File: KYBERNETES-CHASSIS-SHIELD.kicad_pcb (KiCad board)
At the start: 2 copper layers, 53.3 x 57.1 mm, 29 parts, among them J1 ESC, J2 Radio, J3 Encoder, J4 I2C, J5 Servo 1, J6 Servo 2, J7 Servo Regulator 1, J8 Servo Regulator 2, U1 LM4040CEM3-3.0T, U2 LM2903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

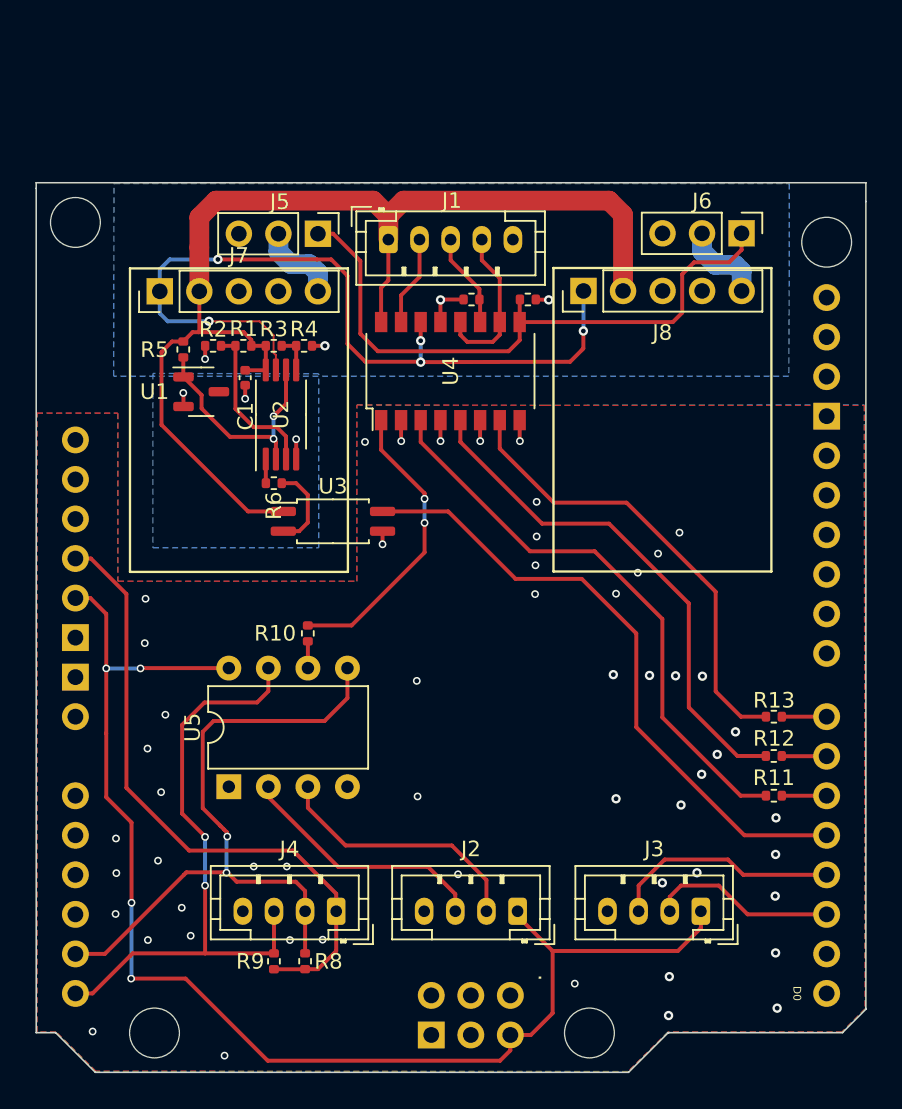
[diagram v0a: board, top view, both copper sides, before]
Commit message: rework into 4 layer board
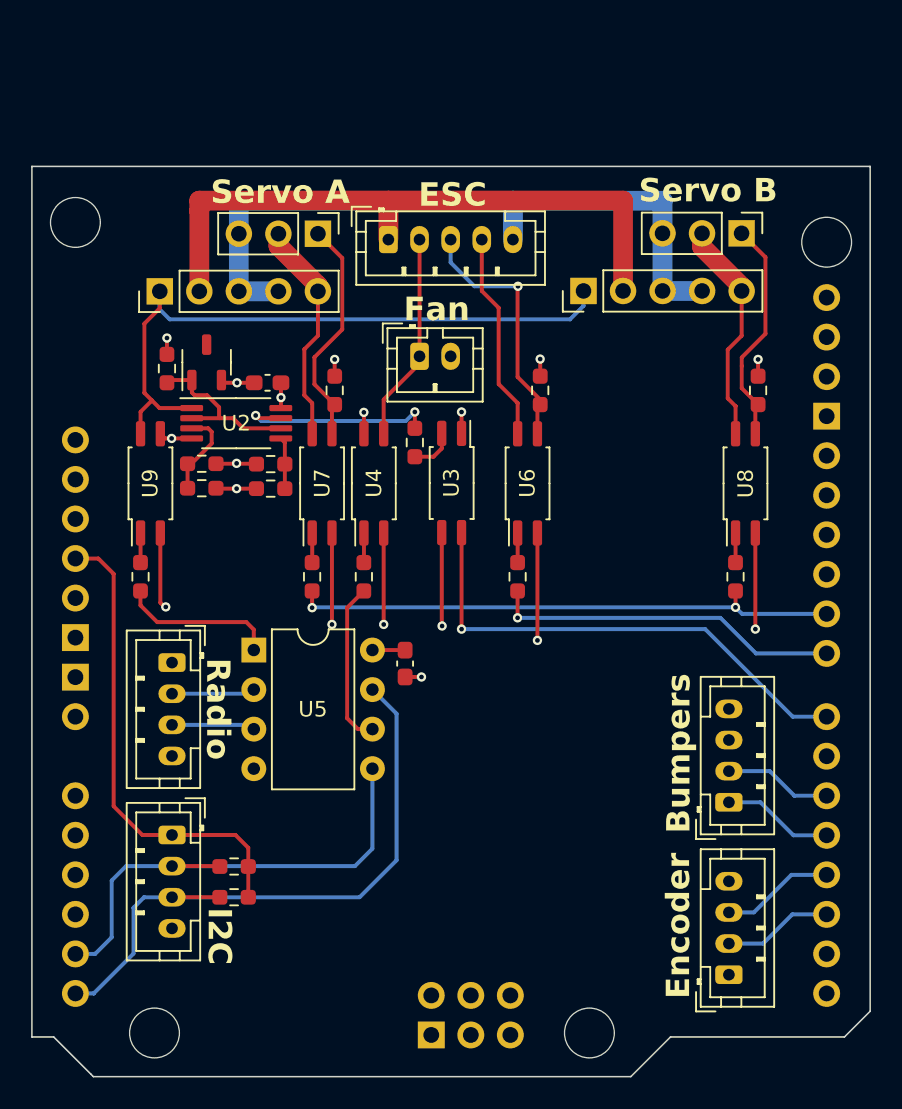
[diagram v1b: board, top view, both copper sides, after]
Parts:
- removed R15: 2k2, Resistor_SMD:R_0402_1005Metric
- added C2: 100n, Capacitor_SMD:C_0603_1608Metric_Pad1.08x0.95mm_HandSolder, F.Cu at (148.8, 105.2)
- added J10: Fan, Connector_JST:JST_PH_B2B-PH-K_1x02_P2.00mm_Vertical, F.Cu at (149.8, 85.5)
- added J5: Bumper, Connector_JST:JST_PH_B4B-PH-K_1x04_P2.00mm_Vertical, F.Cu at (169.7, 114.1)
- added R18: 680, Resistor_SMD:R_0603_1608Metric_Pad0.98x0.95mm_HandSolder, F.Cu at (142.9, 99.6)
- added R19: 680, Resistor_SMD:R_0603_1608Metric_Pad0.98x0.95mm_HandSolder, F.Cu at (131.8, 99.6)
- added R7: 680, Resistor_SMD:R_0603_1608Metric_Pad0.98x0.95mm_HandSolder, F.Cu at (146.2, 99.6)
- added U6: TCMT1104, Package_SO:SOP-4_4.4x2.6mm_P1.27mm, F.Cu at (156.7, 93.6)
- added U7: TCMT1104, Package_SO:SOP-4_4.4x2.6mm_P1.27mm, F.Cu at (143.5, 93.6)
- added U8: TCMT1104, Package_SO:SOP-4_4.4x2.6mm_P1.27mm, F.Cu at (170.7, 93.6)
- added U9: TCMT1104, Package_SO:SOP-4_4.4x2.6mm_P1.27mm, F.Cu at (132.5, 93.6)
- C1: footprint Capacitor_SMD:C_0402_1005Metric -> Capacitor_SMD:C_0603_1608Metric_Pad1.08x0.95mm_HandSolder
- R1, R10, R11, R12, R13, R14, R2, R3, R4, R5, R6, R8, R9: footprint Resistor_SMD:R_0402_1005Metric -> Resistor_SMD:R_0603_1608Metric_Pad0.98x0.95mm_HandSolder
- U4: value TCMT4100 -> TCMT1104; footprint Package_SO:SOP-16_4.4x10.4mm_P1.27mm -> Package_SO:SOP-4_4.4x2.6mm_P1.27mm
- moved R11 30.1 mm to (157.5, 87.6), turned to 90 degrees
- moved J2 27.4 mm to (133.9, 105.1), turned to -90 degrees
- moved R12 20.1 mm to (156.1, 99.6), turned to 90 degrees
- moved R14 15.9 mm to (171.5, 87.6), turned to 90 degrees
- moved R10 15.7 mm to (144.3, 87.6)
- moved J4 11.6 mm to (133.9, 116.2), turned to -90 degrees
- moved R3 10.3 mm to (135.8, 93.9), turned to 180 degrees
- moved R4 10.0 mm to (135.8, 92.3)
- moved R6 9.43 mm to (149.5, 91.0), turned to -90 degrees
- moved R1 9.34 mm to (140.2, 94.0), turned to 0 degrees
- moved R13 9.32 mm to (170.1, 99.6), turned to 90 degrees
- moved U5 8.93 mm to (139.1, 104.3), turned to 0 degrees
- moved U4 8.73 mm to (146.8, 93.6)
- moved R2 8.45 mm to (140.2, 92.4)
- moved U3 8.02 mm to (151.8, 93.6), turned to -90 degrees
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- renumbered J5 to J6, J6 to J7, J7 to J8, J8 to J9
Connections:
- net SERVO_POWER_1 renamed SERVO_1_POWER
- net SERVO_POWER_2 renamed SERVO_2_POWER
- J1 pad 4: +5VP -> ESC_POWER
- J6 pad 1: SERVO_IN -> SERVO_1_IN
- J7 pad 1: SERVO_IN -> SERVO_2_IN
- R10 pad 1: ESC_ENABLE_LOGIC -> SERVO_1_IN
- R10 pad 2: Net-(R10-Pad2) -> GND2
- R11 pad 1: SERVO_DISABLE_LOGIC -> ESC_IN
- R11 pad 2: Net-(R11-Pad2) -> GND2
- R14 pad 1: SERVO_IN -> SERVO_2_IN
- U2 pad 1: Net-(R6-Pad1) -> SERVO_DISABLE
- U2 pad 3: MotorBattLowSense -> MotorBattCritSense
- U2 pad 5: MotorBattCritSense -> MotorBattLowSense
- U2 pad 7: SERVO_DISABLE -> Net-(R6-Pad1)
- U4 pad 1: Net-(R10-Pad2) -> Net-(R7-Pad2)
- U4 pad 3: Net-(R11-Pad2) -> ESC_ENABLE
- U4 pad 4: GND -> +12V
- U5 pad 1: unconnected-(U5-~{RESET}/PB5-Pad1) -> SERVO_DISABLE_LOGIC
- U5 pad 2: RADIO_CH2 -> RADIO_CH1
- U5 pad 3: RADIO_CH1 -> RADIO_CH2
- XA1 pad D4: ~{MotorBattLow} -> BUMPER_A
- XA1 pad D5: SERVO_DISABLE_LOGIC -> BUMPER_B
- XA1 pad D6: ESC_IN_LOGIC -> unconnected-(XA1-PadD6)
- XA1 pad D7: SERVO_IN_LOGIC -> ~{MotorBattLow}
- XA1 pad D8: unconnected-(XA1-PadD8) -> ESC_IN_LOGIC
- XA1 pad D9: unconnected-(XA1-PadD9) -> SERVO_IN_LOGIC
- XA1 pad GND1: GND -> unconnected-(XA1-GND-PadGND1)
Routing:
- net +5V: track 84.2 -> 2.10 mm, vias 4 -> 0
- net GND2: track 8.51 -> 56.6 mm, vias 7 -> 6
- net SERVO_IN: track 40.4 -> 0.00 mm
- net Net-(R11-Pad2): track 36.7 -> 0.00 mm
- net SERVO_IN_LOGIC: track 2.88 -> 35.4 mm, vias 0 -> 2
- net Net-(R12-Pad2): track 33.3 -> 1.90 mm
- net GND: track 6.25 -> 36.8 mm, vias 54 -> 7
- net Net-(R13-Pad2): track 29.8 -> 1.90 mm
- net +12V: track 73.7 -> 49.4 mm, vias 0 -> 5
- net ESC_IN_LOGIC: track 2.89 -> 22.5 mm, vias 0 -> 1
- net Net-(R10-Pad2): track 19.1 -> 0.00 mm, vias 2 -> 0
- net SERVO_1_IN: track 0.00 -> 14.8 mm
- net SERVO_2_IN: track 0.00 -> 14.6 mm
- net ESC_POWER: track 0.00 -> 13.4 mm
- net Net-(R6-Pad1): track 1.55 -> 13.3 mm, vias 0 -> 2
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- added copper zone on In2.Cu, net +12V
- added copper zone on In2.Cu, net +5V
- added copper zone on In1.Cu, net GND
- added copper zone on In1.Cu, net GND2
- removed copper zone on B.Cu, net GND
- removed copper zone on F.Cu, net GND
- removed copper zone on B.Cu, net GND2
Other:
- board size 53.3 x 57.1 mm -> 53.8 x 58.5 mm
- copper layers 2 -> 4
- board text added: "Bumpers"
- board text added: "ESC"
- board text added: "Encoder"
- board text added: "Fan"
- board text added: "I2C"
- board text added: "Radio"
- board text added: "Servo A"
- board text added: "Servo B"

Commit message: version 1.0
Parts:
- moved R10 4.01 mm to (144.3, 91.7)
- moved R11 4.01 mm to (157.5, 91.7)
- moved R14 4.01 mm to (171.5, 91.7)
- moved U4 4.01 mm to (146.8, 97.6)
- moved U6 4.01 mm to (156.7, 97.6)
- moved U7 4.01 mm to (143.5, 97.6)
- moved U8 4.01 mm to (170.7, 97.6)
- moved U9 4.01 mm to (132.5, 97.6)
- moved U3 4.01 mm to (151.8, 97.6)
- moved R18 3.20 mm to (141.9, 102.7), turned to 0 degrees
- moved R12 3.20 mm to (157.0, 102.7), turned to 180 degrees
- moved R13 3.20 mm to (169.2, 102.7), turned to 0 degrees
- moved R7 3.19 mm to (145.3, 102.7), turned to 0 degrees
- moved R19 3.17 mm to (132.8, 102.7), turned to 180 degrees
- moved R6 1.68 mm to (151.0, 91.6)
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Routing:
- net GND: track 36.8 -> 6.29 mm
- net ~{MotorBattLow}: track 32.0 -> 27.6 mm
- net ESC_ENABLE: track 13.4 -> 17.4 mm
- net SERVO_DISABLE: track 42.8 -> 46.8 mm
- net ESC_POWER: track 13.4 -> 17.4 mm
- net SERVO_1_POWER: track 14.5 -> 18.5 mm
- net SERVO_2_POWER: track 14.5 -> 18.5 mm
- net ESC_IN: track 16.6 -> 20.6 mm
- net SERVO_1_IN: track 14.8 -> 18.6 mm
- net ESC_IN_LOGIC: track 22.5 -> 18.8 mm
- net SERVO_2_IN: track 14.6 -> 18.3 mm
- net SERVO_DISABLE_LOGIC: track 10.2 -> 7.27 mm
- net SERVO_IN_LOGIC: track 35.4 -> 37.2 mm
- net ESC_ENABLE_LOGIC: track 10.5 -> 9.10 mm
- net Net-(R6-Pad2): track 2.92 -> 1.94 mm
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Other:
- board text added: "Battery Critical Reference"
- board text added: "Battery Low Reference"
- board text added: "Kybernetes 2 Shield"

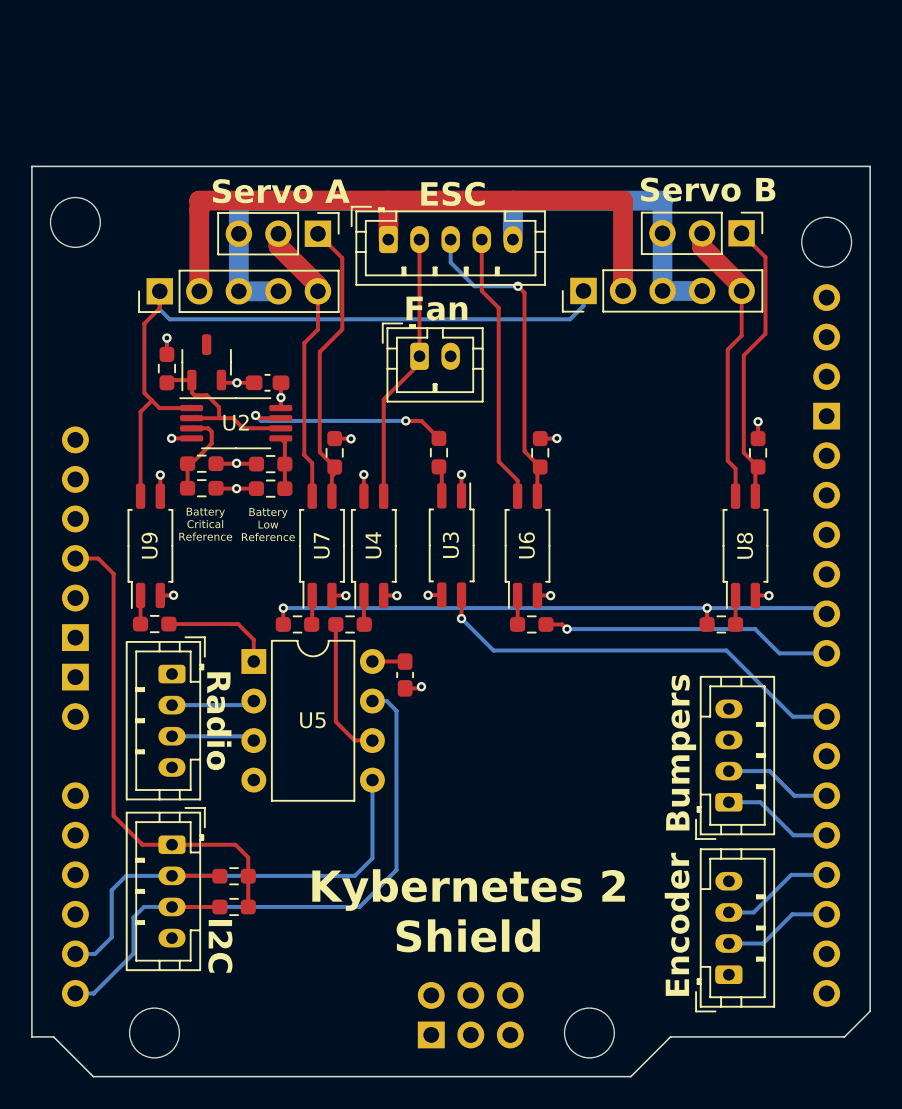
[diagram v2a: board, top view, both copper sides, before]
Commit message: add comparator bias resistor, increase low voltage thresholds, add large capacitors for servos
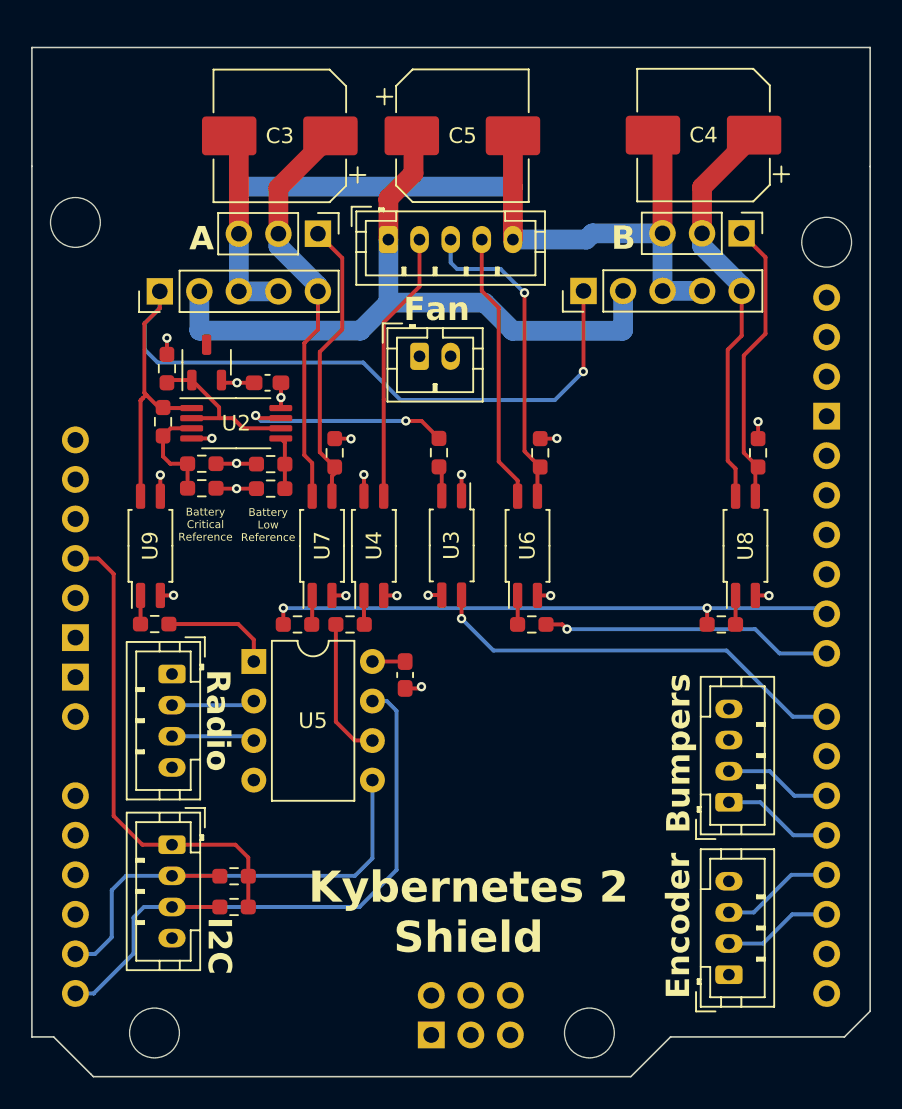
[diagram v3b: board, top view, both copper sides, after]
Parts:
- added C3: 470u, Capacitor_SMD:CP_Elec_8x10, F.Cu at (140.8, 71.3)
- added C4: 470u, Capacitor_SMD:CP_Elec_8x10, F.Cu at (168.0, 71.2)
- added C5: 470u, Capacitor_SMD:CP_Elec_8x10, F.Cu at (152.5, 71.3)
- added R15: 1M, Resistor_SMD:R_0603_1608Metric_Pad0.98x0.95mm_HandSolder, F.Cu at (133.3, 89.7)
- R1: value 44k2 -> 48k7
- R3: value 37k4 -> 44k2
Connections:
- J10 pad 1: ESC_ENABLE -> +12V
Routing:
- net GND2: track 57.1 -> 76.8 mm
- net SERVO_DISABLE: track 46.8 -> 56.9 mm, vias 0 -> 1
- net SERVO_2_POWER: track 18.5 -> 26.4 mm
- net SERVO_1_POWER: track 18.5 -> 26.2 mm
- net +12V: track 49.4 -> 53.3 mm
- net MotorBattCritSense: track 5.79 -> 6.70 mm
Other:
- board size 53.8 x 58.5 mm -> 53.8 x 66.1 mm
- board text added: "A"
- board text added: "B"
- board text removed: "ESC"
- board text removed: "Servo A"
- board text removed: "Servo B"

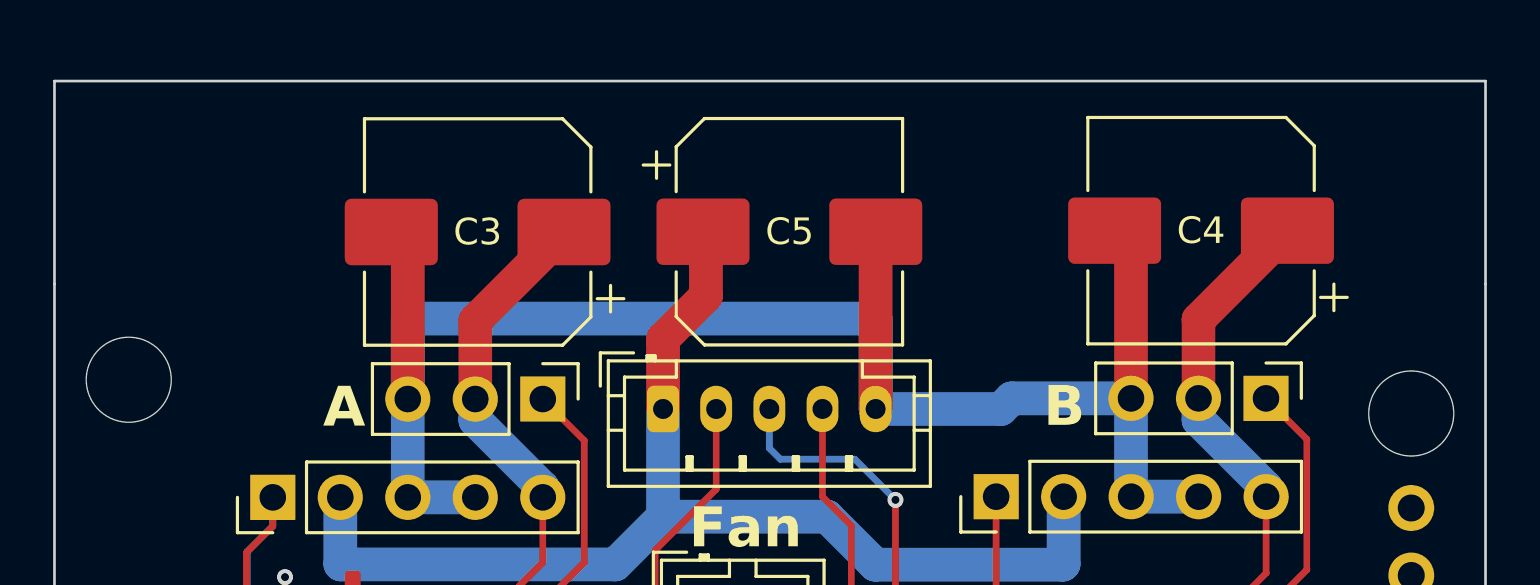
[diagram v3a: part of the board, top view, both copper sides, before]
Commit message: fix the incorrect footprint for desired capacitors (wurth 875115357006)
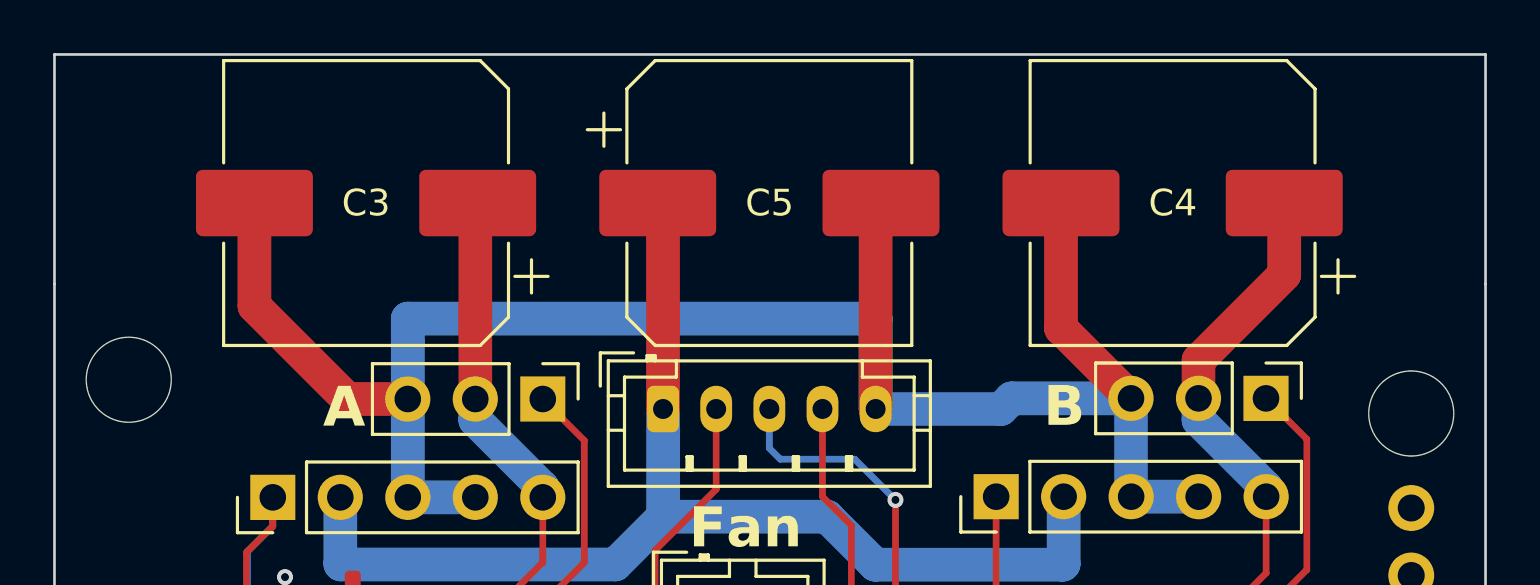
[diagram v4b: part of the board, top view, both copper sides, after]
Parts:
- C3, C4, C5: footprint Capacitor_SMD:CP_Elec_8x10 -> Capacitor_SMD:CP_Elec_10x10.5
- moved C3 4.34 mm to (136.6, 70.2)
- moved C4 1.49 mm to (166.9, 70.2)
- moved C5 1.32 mm to (151.8, 70.2)
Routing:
- net GND2: track 76.8 -> 84.3 mm
- net SERVO_2_POWER: track 26.4 -> 27.4 mm
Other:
- board size 53.8 x 66.1 mm -> 53.8 x 67.1 mm
